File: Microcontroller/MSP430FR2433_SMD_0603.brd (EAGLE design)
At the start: 160 x 100 mm, 9 parts, among them IC1 MSP430FR2433IRGET, IC2 MSP430FR2433IRGET, Y1 32.768kHz

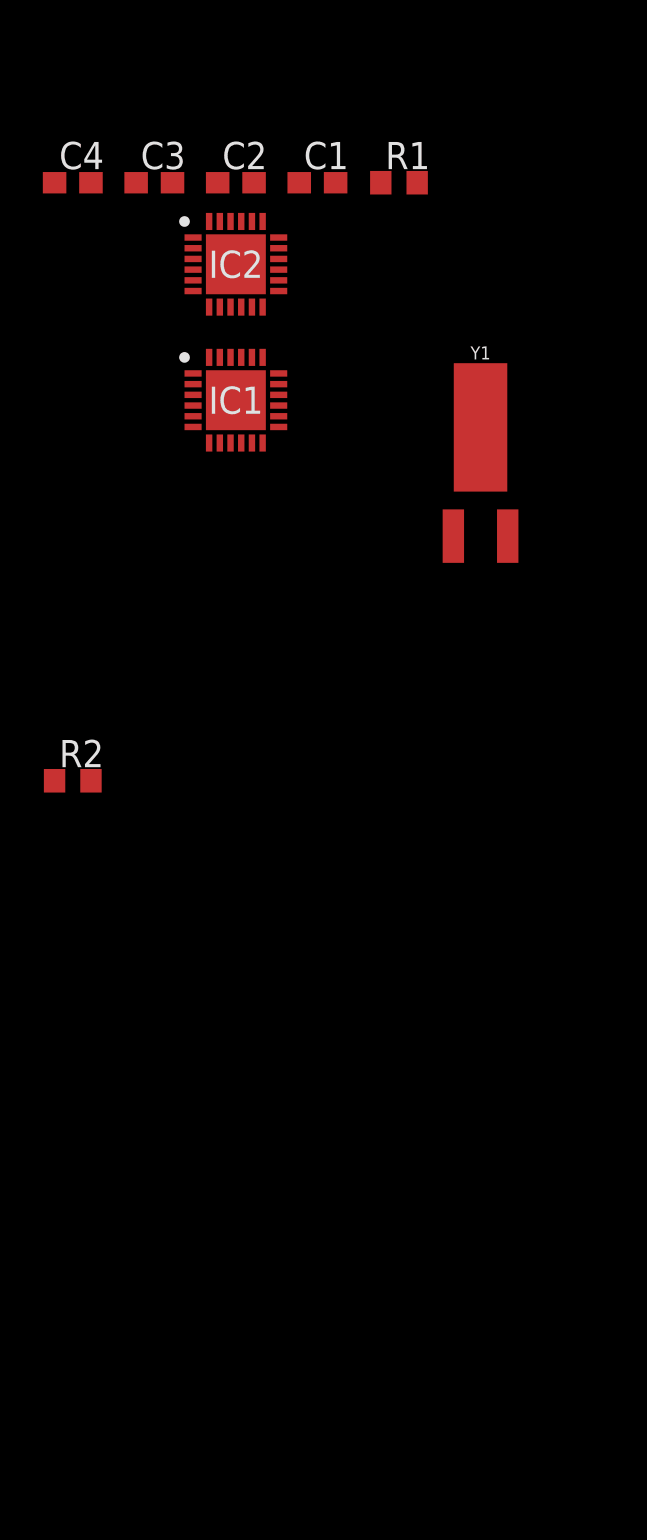
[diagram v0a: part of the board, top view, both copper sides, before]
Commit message: msp430fr2433 added
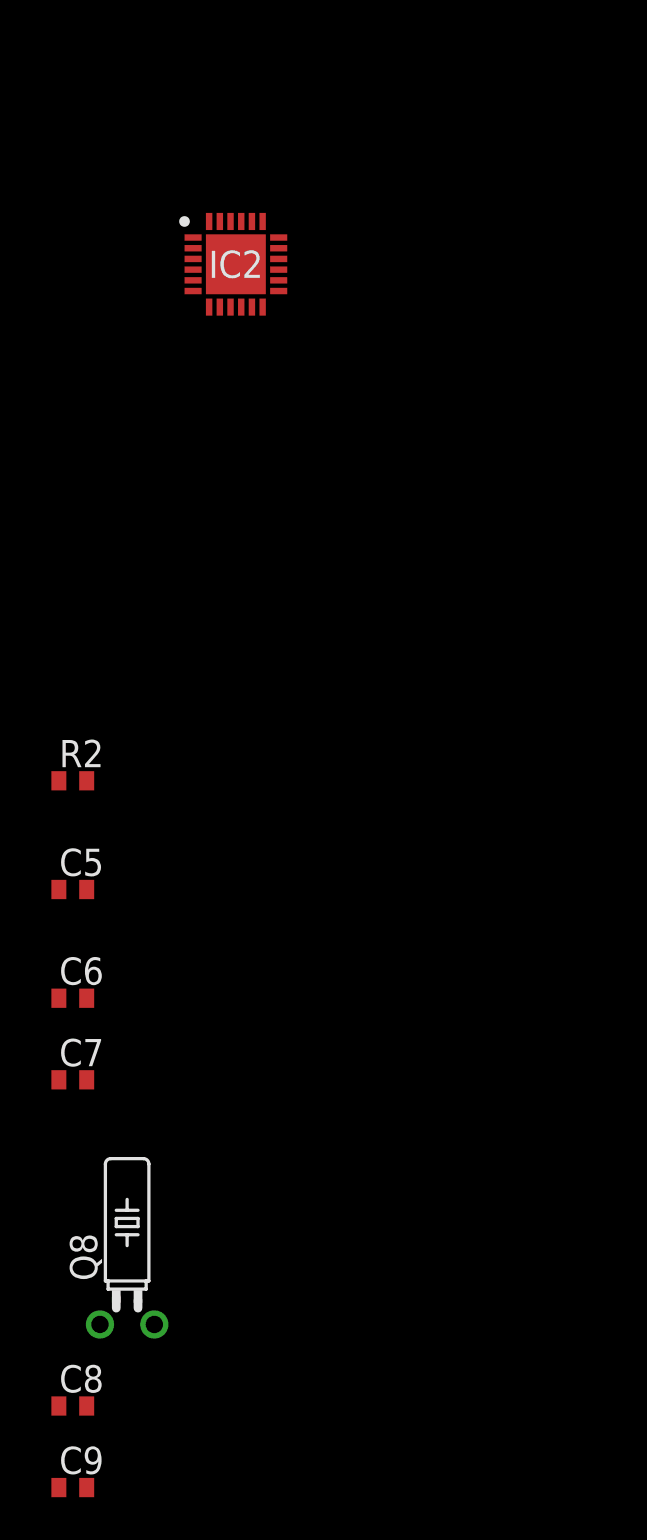
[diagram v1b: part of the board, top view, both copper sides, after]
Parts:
- removed C1, C2, C3, C4: (no value), rcl:C0603
- removed IC1: MSP430FR2433IRGET, SamacSys_Parts:QFN50P400X400X100-25N
- removed R1: (no value), rcl:R0603
- removed Y1: 32.768kHz, SparkFun-Clocks:CRYSTAL-SMD-2X6-CYL
- added C5: 1.1n, rcl:C0402
- added C6: 4.7u, rcl:C0402
- added C7: 100n, rcl:C0402
- added C8, C9: 9p, rcl:C0402
- added Q8: 32.768, crystal:TC26H
- R2: value (none) -> 47K; device rcl:R0603 -> rcl:R0402
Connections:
- removed net N$1: IC2.1, R2.1
- removed net N$5: C1.2, IC1.22, Y1.X1
- removed net N$6: C2.2, IC1.21, Y1.X2
- removed net P1.0: IC1.7
- removed net P1.1: IC1.8
- removed net P1.2: IC1.9
- removed net P1.3: IC1.10
- removed net P1.4: IC1.3
- removed net P1.5: IC1.4
- removed net P1.6: IC1.5
- removed net P1.7: IC1.6
- removed net P2.2: IC1.11
- removed net P2.7: IC1.19
- removed net P3.0: IC1.12
- removed net P3.2: IC1.20
- new net ACLK: IC2.15
- new net MISO: IC2.16
- new net MOSI: IC2.17
- new net MSPVCC: C6.1, C7.1, IC2.18, IC2.23, IC2.24
- new net N$10: IC2.8
- new net N$11: IC2.9
- new net N$12: IC2.10
- new net N$13: IC2.11
- new net N$14: IC2.12
- new net N$20: IC2.20
- new net N$21: IC2.19
- new net N$26: IC2.14
- new net N$27: IC2.13
- new net N$9: IC2.7
- new net RXD: IC2.4
- new net TDI: IC2.5
- new net TDO: IC2.6
- new net TXD: IC2.3
- new net XIN: C8.1, IC2.22, Q8.2
- new net XOUT: C9.1, IC2.21, Q8.1
- net GND: now also C5.2, C6.2, C7.2, C8.2, C9.2, IC2.25; no longer C1.1, C2.1, C3.2, C4.2, IC1.18, IC1.23, IC1.25
- net RESET: now also C5.1, IC2.1, R2.1; no longer IC1.1, R1.1
- net TEST: now also IC2.2; no longer IC1.2
- net VCC: now also R2.2; no longer C3.1, C4.1, IC1.24, R1.2

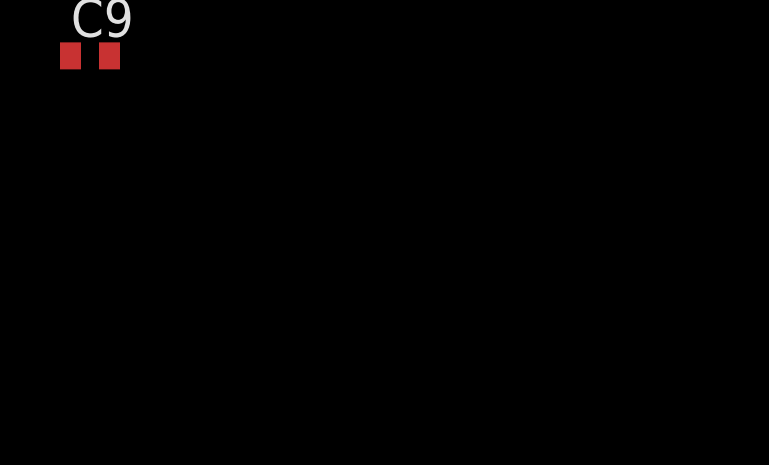
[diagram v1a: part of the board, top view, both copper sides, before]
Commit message: masp430fr2433 modified
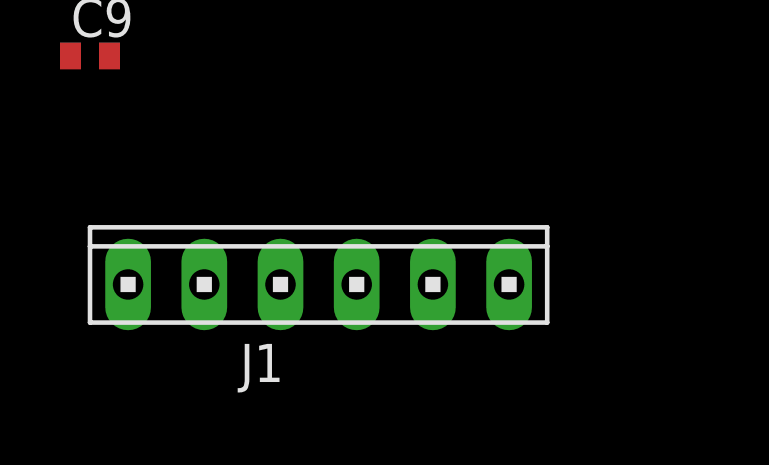
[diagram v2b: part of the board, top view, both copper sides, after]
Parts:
- added J1: (no value), con-amp:10X06MTA
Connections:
- net GND: now also J1.5
- net RESET: now also J1.2
- net RXD: now also J1.3
- net TEST: now also J1.1
- net TXD: now also J1.4
- net VCC: now also J1.6
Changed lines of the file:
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@@
 <element name="C8" library="rcl" package="C0402" value="9p" x="-30.48" y="-31.75"/>
 <element name="C9" library="rcl" package="C0402" value="9p" x="-30.48" y="-35.56"/>
+<element name="J1" library="con-amp" package="10X06MTA" value="" x="-22.86" y="-43.18"/>
 </elements>
 <signals>
@@
 <contactref element="R2" pad="1"/>
 <contactref element="IC2" pad="1"/>
+<contactref element="J1" pad="2"/>
+<wire x1="-31.13" y1="-7.62" x2="-19.05" y2="-43.18" width="0" layer="19" extent="1-1"/>
 <wire x1="-31.13" y1="-2.54" x2="-31.13" y2="-7.62" width="0" layer="19" extent="1-1"/>
 <wire x1="-24.86" y1="22.84" x2="-31.13" y2="-2.54" width="0" layer="19" extent="1-1"/>
@@
 <contactref element="C9" pad="2"/>
 <contactref element="IC2" pad="25"/>
+<contactref element="J1" pad="5"/>
+<wire x1="-29.83" y1="-35.56" x2="-26.67" y2="-43.18" width="0" layer="19" extent="1-1"/>
 <wire x1="-29.83" y1="-31.75" x2="-29.83" y2="-35.56" width="0" layer="19" extent="1-1"/>
 <wire x1="-29.83" y1="-16.51" x2="-29.83" y2="-31.75" width="0" layer="19" extent="1-1"/>
@@
 <signal name="VCC">
 <contactref element="R2" pad="2"/>
+<contactref element="J1" pad="6"/>
+<wire x1="-29.83" y1="-2.54" x2="-29.21" y2="-43.18" width="0" layer="19" extent="1-1"/>
 </signal>
 <signal name="TEST">
 <contactref element="IC2" pad="2"/>
+<contactref element="J1" pad="1"/>
+<wire x1="-24.86" y1="22.34" x2="-16.51" y2="-43.18" width="0" layer="19" extent="1-1"/>
 </signal>
 <signal name="TXD">
 <contactref element="IC2" pad="3"/>
+<contactref element="J1" pad="4"/>
+<wire x1="-24.86" y1="21.84" x2="-24.13" y2="-43.18" width="0" layer="19" extent="1-1"/>
 </signal>
 <signal name="RXD">
 <contactref element="IC2" pad="4"/>
+<contactref element="J1" pad="3"/>
+<wire x1="-24.86" y1="21.34" x2="-21.59" y2="-43.18" width="0" layer="19" extent="1-1"/>
 </signal>
 <signal name="TDI">

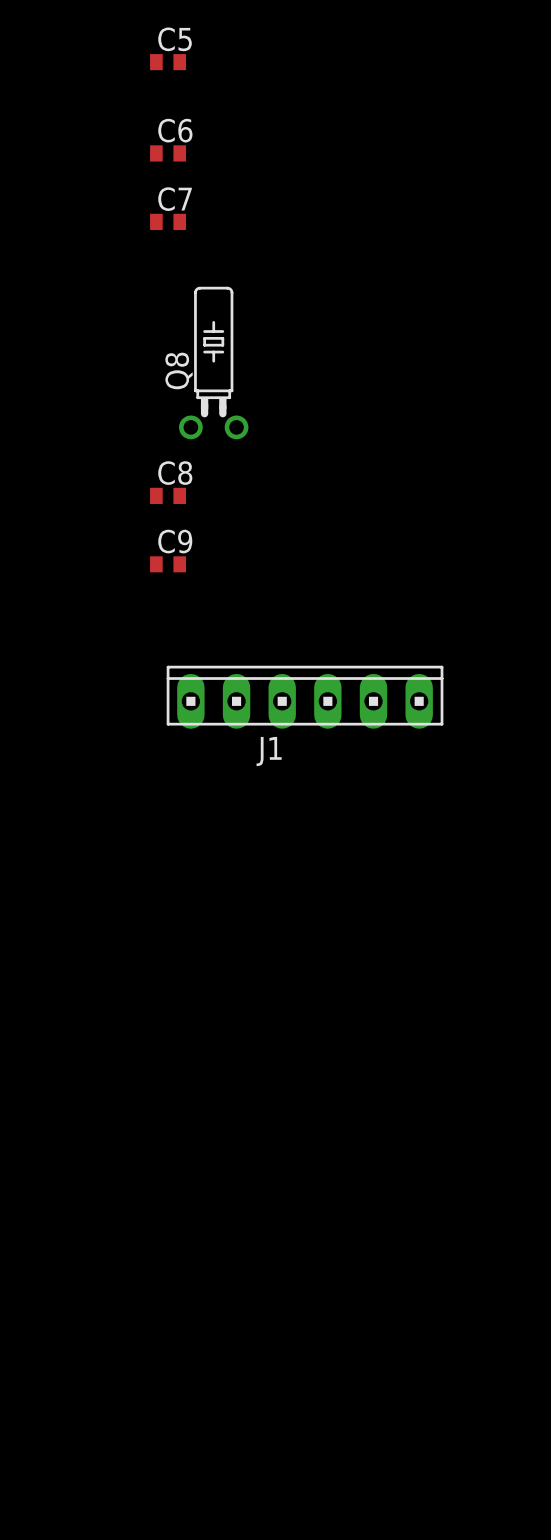
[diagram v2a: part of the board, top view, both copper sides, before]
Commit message: masp430fr2433 modified
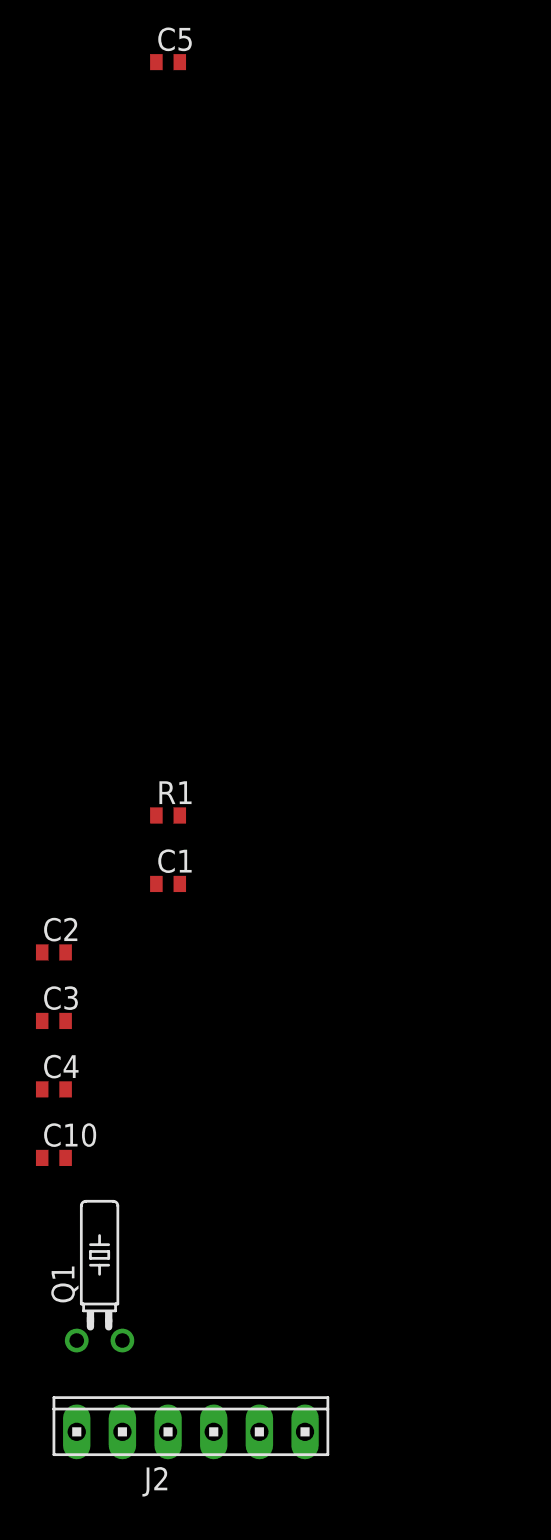
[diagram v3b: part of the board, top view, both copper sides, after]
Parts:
- removed C6: 4.7u, rcl:C0402
- removed C7: 100n, rcl:C0402
- removed C8, C9: 9p, rcl:C0402
- removed J1: (no value), con-amp:10X06MTA
- removed Q8: 32.768, crystal:TC26H
- added C1: (no value), rcl:C0402
- added C10: 100n, rcl:C0402
- added C2, C3: 9p, rcl:C0402
- added C4: 4.7u, rcl:C0402
- added J2: (no value), con-amp:10X06MTA
- added Q1: 32.768, crystal:TC26H
- added R1: 47k, rcl:R0402
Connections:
- net N$11 renamed SDA
- net N$12 renamed SCL
- net TDI renamed N$7
- net TDO renamed N$8
- removed net MSPVCC: C6.1, C7.1, IC2.18, IC2.23, IC2.24
- removed net XIN: C8.1, IC2.22, Q8.2
- new net N$3: C3.1, IC2.22, Q1.2
- net GND: now also C1.2, C10.2, C2.2, C3.2, C4.2, J2.5; no longer C6.2, C7.2, C8.2, C9.2, J1.5
- net RESET: now also C1.1, J2.1, R1.1; no longer J1.2
- net RXD: now also J2.3; no longer J1.3
- net TEST: now also J2.2; no longer J1.1
- net TXD: now also J2.4; no longer J1.4
- net VCC: now also C10.1, C4.1, IC2.18, IC2.23, IC2.24, J2.6, R1.2; no longer J1.6
- net XOUT: now also C2.1, Q1.1; no longer C9.1, Q8.1
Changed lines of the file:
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@@
 <element name="R2" library="rcl" package="R0402" value="47K" x="-30.48" y="-2.54"/>
 <element name="C5" library="rcl" package="C0402" value="1.1n" x="-30.48" y="-7.62"/>
-<element name="C6" library="rcl" package="C0402" value="4.7u" x="-30.48" y="-12.7"/>
-<element name="C7" library="rcl" package="C0402" value="100n" x="-30.48" y="-16.51"/>
-<element name="Q8" library="crystal" package="TC26H" value="32.768" x="-27.94" y="-27.94"/>
-<element name="C8" library="rcl" package="C0402" value="9p" x="-30.48" y="-31.75"/>
-<element name="C9" library="rcl" package="C0402" value="9p" x="-30.48" y="-35.56"/>
-<element name="J1" library="con-amp" package="10X06MTA" value="" x="-22.86" y="-43.18"/>
+<element name="R1" library="rcl" package="R0402" value="47k" x="-30.48" y="-49.53"/>
+<element name="C1" library="rcl" package="C0402" value="" x="-30.48" y="-53.34"/>
+<element name="C2" library="rcl" package="C0402" value="9p" x="-36.83" y="-57.15"/>
+<element name="C3" library="rcl" package="C0402" value="9p" x="-36.83" y="-60.96"/>
+<element name="C4" library="rcl" package="C0402" value="4.7u" x="-36.83" y="-64.77"/>
+<element name="C10" library="rcl" package="C0402" value="100n" x="-36.83" y="-68.58"/>
+<element name="Q1" library="crystal" package="TC26H" value="32.768" x="-34.29" y="-78.74"/>
+<element name="J2" library="con-amp" package="10X06MTA" value="" x="-29.21" y="-83.82"/>
 </elements>
 <signals>
@@
 <contactref element="R2" pad="1"/>
 <contactref element="IC2" pad="1"/>
-<contactref element="J1" pad="2"/>
-<wire x1="-31.13" y1="-7.62" x2="-19.05" y2="-43.18" width="0" layer="19" extent="1-1"/>
+<contactref element="R1" pad="1"/>
+<contactref element="C1" pad="1"/>
+<contactref element="J2" pad="1"/>
+<wire x1="-31.13" y1="-53.34" x2="-22.86" y2="-83.82" width="0" layer="19" extent="1-1"/>
+<wire x1="-31.13" y1="-49.53" x2="-31.13" y2="-53.34" width="0" layer="19" extent="1-1"/>
+<wire x1="-31.13" y1="-7.62" x2="-31.13" y2="-49.53" width="0" layer="19" extent="1-1"/>
 <wire x1="-31.13" y1="-2.54" x2="-31.13" y2="-7.62" width="0" layer="19" extent="1-1"/>
 <wire x1="-24.86" y1="22.84" x2="-31.13" y2="-2.54" width="0" layer="19" extent="1-1"/>
@@
 <signal name="GND">
 <contactref element="C5" pad="2"/>
-<contactref element="C6" pad="2"/>
-<contactref element="C7" pad="2"/>
-<contactref element="C8" pad="2"/>
-<contactref element="C9" pad="2"/>
 <contactref element="IC2" pad="25"/>
-<contactref element="J1" pad="5"/>
-<wire x1="-29.83" y1="-35.56" x2="-26.67" y2="-43.18" width="0" layer="19" extent="1-1"/>
-<wire x1="-29.83" y1="-31.75" x2="-29.83" y2="-35.56" width="0" layer="19" extent="1-1"/>
-<wire x1="-29.83" y1="-16.51" x2="-29.83" y2="-31.75" width="0" layer="19" extent="1-1"/>
-<wire x1="-29.83" y1="-12.7" x2="-29.83" y2="-16.51" width="0" layer="19" extent="1-1"/>
-<wire x1="-29.83" y1="-7.62" x2="-29.83" y2="-12.7" width="0" layer="19" extent="1-1"/>
+<contactref element="C1" pad="2"/>
+<contactref element="C4" pad="2"/>
+<contactref element="C10" pad="2"/>
+<contactref element="C3" pad="2"/>
+<contactref element="C2" pad="2"/>
+<contactref element="J2" pad="5"/>
+<wire x1="-36.18" y1="-68.58" x2="-33.02" y2="-83.82" width="0" layer="19" extent="1-1"/>
+<wire x1="-36.18" y1="-64.77" x2="-36.18" y2="-68.58" width="0" layer="19" extent="1-1"/>
+<wire x1="-36.18" y1="-60.96" x2="-36.18" y2="-64.77" width="0" layer="19" extent="1-1"/>
+<wire x1="-36.18" y1="-57.15" x2="-36.18" y2="-60.96" width="0" layer="19" extent="1-1"/>
+<wire x1="-29.83" y1="-53.34" x2="-36.18" y2="-57.15" width="0" layer="19" extent="1-1"/>
+<wire x1="-29.83" y1="-7.62" x2="-29.83" y2="-53.34" width="0" layer="19" extent="1-1"/>
 <wire x1="-22.86" y1="21.59" x2="-29.83" y2="-7.62" width="0" layer="19" extent="1-1"/>
 </signal>
 <signal name="VCC">
 <contactref element="R2" pad="2"/>
-<contactref element="J1" pad="6"/>
-<wire x1="-29.83" y1="-2.54" x2="-29.21" y2="-43.18" width="0" layer="19" extent="1-1"/>
+<contactref element="R1" pad="2"/>
+<contactref element="IC2" pad="23"/>
+<contactref element="IC2" pad="24"/>
+<contactref element="C4" pad="1"/>
+<contactref element="C10" pad="1"/>
+<contactref element="IC2" pad="18"/>
+<contactref element="J2" pad="6"/>
+<wire x1="-37.48" y1="-68.58" x2="-35.56" y2="-83.82" width="0" layer="19" extent="1-1"/>
+<wire x1="-37.48" y1="-64.77" x2="-37.48" y2="-68.58" width="0" layer="19" extent="1-1"/>
+<wire x1="-29.83" y1="-49.53" x2="-37.48" y2="-64.77" width="0" layer="19" extent="1-1"/>
+<wire x1="-29.83" y1="-2.54" x2="-29.83" y2="-49.53" width="0" layer="19" extent="1-1"/>
+<wire x1="-24.11" y1="23.59" x2="-29.83" y2="-2.54" width="0" layer="19" extent="1-1"/>
+<wire x1="-23.61" y1="23.59" x2="-24.11" y2="23.59" width="0" layer="19" extent="1-1"/>
+<wire x1="-20.86" y1="22.84" x2="-23.61" y2="23.59" width="0" layer="19" extent="1-1"/>
+</signal>
+<signal name="XOUT">
+<contactref element="IC2" pad="21"/>
+<contactref element="Q1" pad="1"/>
+<contactref element="C2" pad="1"/>
+<wire x1="-37.48" y1="-57.15" x2="-35.56" y2="-78.74" width="0" layer="19" extent="1-1"/>
+<wire x1="-22.61" y1="23.59" x2="-37.48" y2="-57.15" width="0" layer="19" extent="1-1"/>
+</signal>
+<signal name="N$3">
+<contactref element="IC2" pad="22"/>
+<contactref element="Q1" pad="2"/>
+<contactref element="C3" pad="1"/>
+<wire x1="-37.48" y1="-60.96" x2="-33.02" y2="-78.74" width="0" layer="19" extent="1-1"/>
+<wire x1="-23.11" y1="23.59" x2="-37.48" y2="-60.96" width="0" layer="19" extent="1-1"/>
 </signal>
 <signal name="TEST">
 <contactref element="IC2" pad="2"/>
-<contactref element="J1" pad="1"/>
-<wire x1="-24.86" y1="22.34" x2="-16.51" y2="-43.18" width="0" layer="19" extent="1-1"/>
+<contactref element="J2" pad="2"/>
+<wire x1="-24.86" y1="22.34" x2="-25.4" y2="-83.82" width="0" layer="19" extent="1-1"/>
 </signal>
 <signal name="TXD">
 <contactref element="IC2" pad="3"/>
-<contactref element="J1" pad="4"/>
-<wire x1="-24.86" y1="21.84" x2="-24.13" y2="-43.18" width="0" layer="19" extent="1-1"/>
+<contactref element="J2" pad="4"/>
+<wire x1="-24.86" y1="21.84" x2="-30.48" y2="-83.82" width="0" layer="19" extent="1-1"/>
 </signal>
 <signal name="RXD">
 <contactref element="IC2" pad="4"/>
-<contactref element="J1" pad="3"/>
-<wire x1="-24.86" y1="21.34" x2="-21.59" y2="-43.18" width="0" layer="19" extent="1-1"/>
+<contactref element="J2" pad="3"/>
+<wire x1="-24.86" y1="21.34" x2="-27.94" y2="-83.82" width="0" layer="19" extent="1-1"/>
 </signal>
-<signal name="TDI">
+<signal name="N$7">
 <contactref element="IC2" pad="5"/>
 </signal>
-<signal name="TDO">
+<signal name="N$8">
 <contactref element="IC2" pad="6"/>
 </signal>
@@
 <contactref element="IC2" pad="8"/>
 </signal>
-<signal name="N$11">
+<signal name="SDA">
 <contactref element="IC2" pad="9"/>
 </signal>
-<signal name="N$12">
+<signal name="SCL">
 <contactref element="IC2" pad="10"/>
 </signal>
@@
 <contactref element="IC2" pad="12"/>
 </signal>
-<signal name="XIN">
-<contactref element="IC2" pad="22"/>
-<contactref element="Q8" pad="2"/>
-<contactref element="C8" pad="1"/>
-<wire x1="-26.67" y1="-27.94" x2="-31.13" y2="-31.75" width="0" layer="19" extent="1-1"/>
-<wire x1="-23.11" y1="23.59" x2="-26.67" y2="-27.94" width="0" layer="19" extent="1-1"/>
-</signal>
-<signal name="XOUT">
-<contactref element="IC2" pad="21"/>
-<contactref element="Q8" pad="1"/>
-<contactref element="C9" pad="1"/>
-<wire x1="-29.21" y1="-27.94" x2="-31.13" y2="-35.56" width="0" layer="19" extent="1-1"/>
-<wire x1="-22.61" y1="23.59" x2="-29.21" y2="-27.94" width="0" layer="19" extent="1-1"/>
-</signal>
-<signal name="N$20">
+<signal name="N$15">
 <contactref element="IC2" pad="20"/>
 </signal>
-<signal name="N$21">
+<signal name="N$16">
 <contactref element="IC2" pad="19"/>
 </signal>
@@
 <contactref element="IC2" pad="15"/>
 </signal>
-<signal name="N$26">
+<signal name="N$21">
 <contactref element="IC2" pad="14"/>
 </signal>
-<signal name="N$27">
+<signal name="N$22">
 <contactref element="IC2" pad="13"/>
 </signal>
-<signal name="MSPVCC">
-<contactref element="IC2" pad="18"/>
-<contactref element="IC2" pad="24"/>
-<contactref element="IC2" pad="23"/>
-<contactref element="C6" pad="1"/>
-<contactref element="C7" pad="1"/>
-<wire x1="-31.13" y1="-12.7" x2="-31.13" y2="-16.51" width="0" layer="19" extent="1-1"/>
-<wire x1="-24.11" y1="23.59" x2="-31.13" y2="-12.7" width="0" layer="19" extent="1-1"/>
-<wire x1="-23.61" y1="23.59" x2="-24.11" y2="23.59" width="0" layer="19" extent="1-1"/>
-<wire x1="-20.86" y1="22.84" x2="-23.61" y2="23.59" width="0" layer="19" extent="1-1"/>
-</signal>
 </signals>

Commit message: masp430fr2433 modified
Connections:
- net ACLK renamed CLK_A1
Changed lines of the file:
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@@
 <contactref element="IC2" pad="16"/>
 </signal>
-<signal name="ACLK">
+<signal name="CLK_A1">
 <contactref element="IC2" pad="15"/>
 </signal>
